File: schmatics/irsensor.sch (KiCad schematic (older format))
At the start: 11 parts, among them Q1 NPN, Q2 NPN

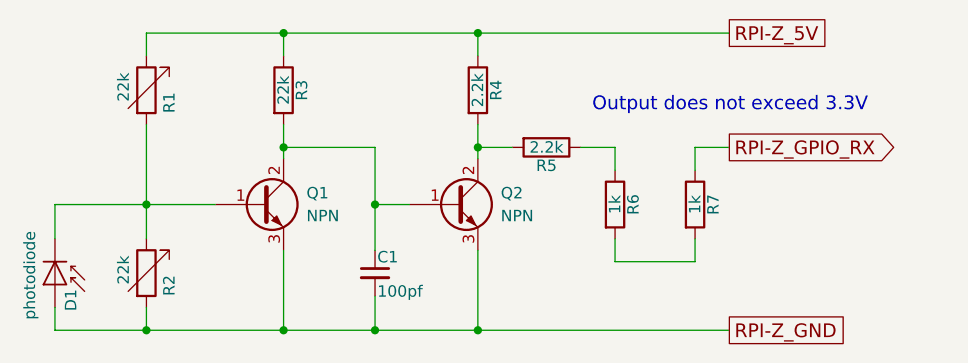
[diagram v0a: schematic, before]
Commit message: add safety resistor to protect the transistor
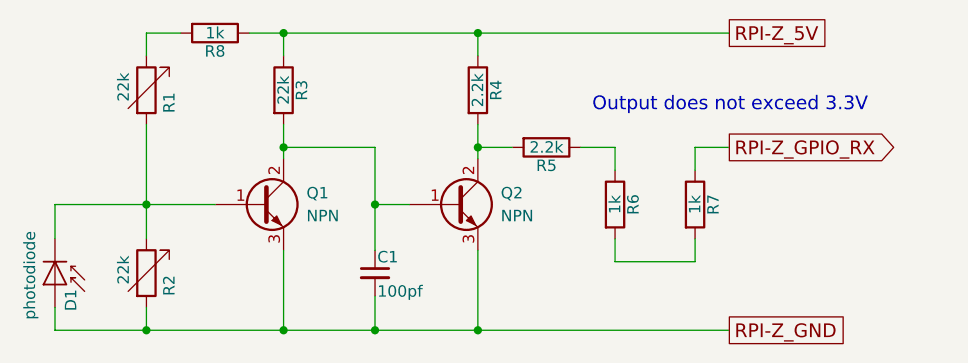
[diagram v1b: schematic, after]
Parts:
- added R8: 1k, symbol R
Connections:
- net RPI-Z_5V: now also R8.1; no longer R1.1
- new net: R1.1, R8.2
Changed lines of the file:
@@
 LIBS:contrib
 LIBS:valves
+LIBS:irsensor-cache
 EELAYER 25 0
 EELAYER END
@@
 Connection ~ 3600 2600
 Wire Wire Line
-	3600 1850 6150 1850
+	4050 1850 6150 1850
 Wire Wire Line
 	4200 1850 4200 1950
@@
 Text Notes 5550 2200 0    60   ~ 0
 Output does not exceed 3.3V
+$Comp
+L R R8
+U 1 1 5E05F263
+P 3900 1850
+F 0 "R8" V 3980 1850 50  0000 C CNN
+F 1 "1k" V 3900 1850 50  0000 C CNN
+F 2 "" V 3830 1850 50  0001 C CNN
+F 3 "" H 3900 1850 50  0001 C CNN
+	1    3900 1850
+	0    1    1    0
+$EndComp
+Wire Wire Line
+	3600 1850 3750 1850
 $EndSCHEMATC
